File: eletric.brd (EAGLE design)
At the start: 100 x 106.7 mm, 13 parts, among them U1 ATTINY85-20PU

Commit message: smyle?
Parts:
- moved R7 4.96 mm to (61.0, 84.5), turned to 195 degrees
- moved R6 3.70 mm to (56.5, 83.2), turned to 190 degrees
- moved R2 3.42 mm to (38.1, 84.5), turned to 165 degrees
- moved R4 2.84 mm to (47.0, 82.5), turned to 175 degrees
- moved R5 2.84 mm to (52.1, 82.5), turned to 185 degrees
- moved R3 2.69 mm to (42.5, 83.2), turned to 170 degrees
- moved LED2 1.27 mm to (49.5, 91.4)
- moved U1 1.27 mm to (45.7, 67.3)
- moved LS1 0.63 mm to (49.5, 5.71)

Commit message: order components && init pcb trail
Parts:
- moved LS1 45.7 mm to (49.5, 51.4), turned to 180 degrees
- moved LS2 43.8 mm to (49.5, 6.99), turned to 180 degrees
- moved LS3 16.5 mm to (49.5, 34.3), turned to 180 degrees
- moved LS4 15.9 mm to (49.5, 19.7), turned to 180 degrees
- moved R2 2.01 mm to (38.7, 86.4), turned to 135 degrees
- moved R7 2.01 mm to (60.3, 86.4), turned to 225 degrees
- moved R3 0.63 mm to (42.5, 83.8), turned to 155 degrees
- moved R6 0.63 mm to (56.5, 83.8), turned to 205 degrees
- turned R4 to 170 degrees
- turned R5 to 190 degrees
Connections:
- net BUZER_HARMONY_1: now also U1.7; no longer U1.5
- net BUZER_HARMONY_3: now also U1.5; no longer U1.7
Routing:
- net BUZER_HARMONY_1: track 0.00 -> 91.9 mm
- net N$3: track 0.00 -> 88.8 mm
- net N$2: track 0.00 -> 74.5 mm
- net BUZER_HARMONY_2: track 0.00 -> 68.4 mm
- net VOLUME: track 0.00 -> 62.9 mm
- net N$4: track 0.00 -> 62.5 mm
- net N$6: track 0.00 -> 60.4 mm
- net VCC: track 0.00 -> 57.5 mm
- net BUZER_HARMONY_3: track 0.00 -> 53.9 mm
- net GND: track 0.00 -> 46.5 mm
- net BUZER_MELODY: track 0.00 -> 43.8 mm
- net RESET: track 0.00 -> 40.0 mm
- net LED: track 0.00 -> 19.6 mm
- net N$5: track 0.00 -> 18.0 mm

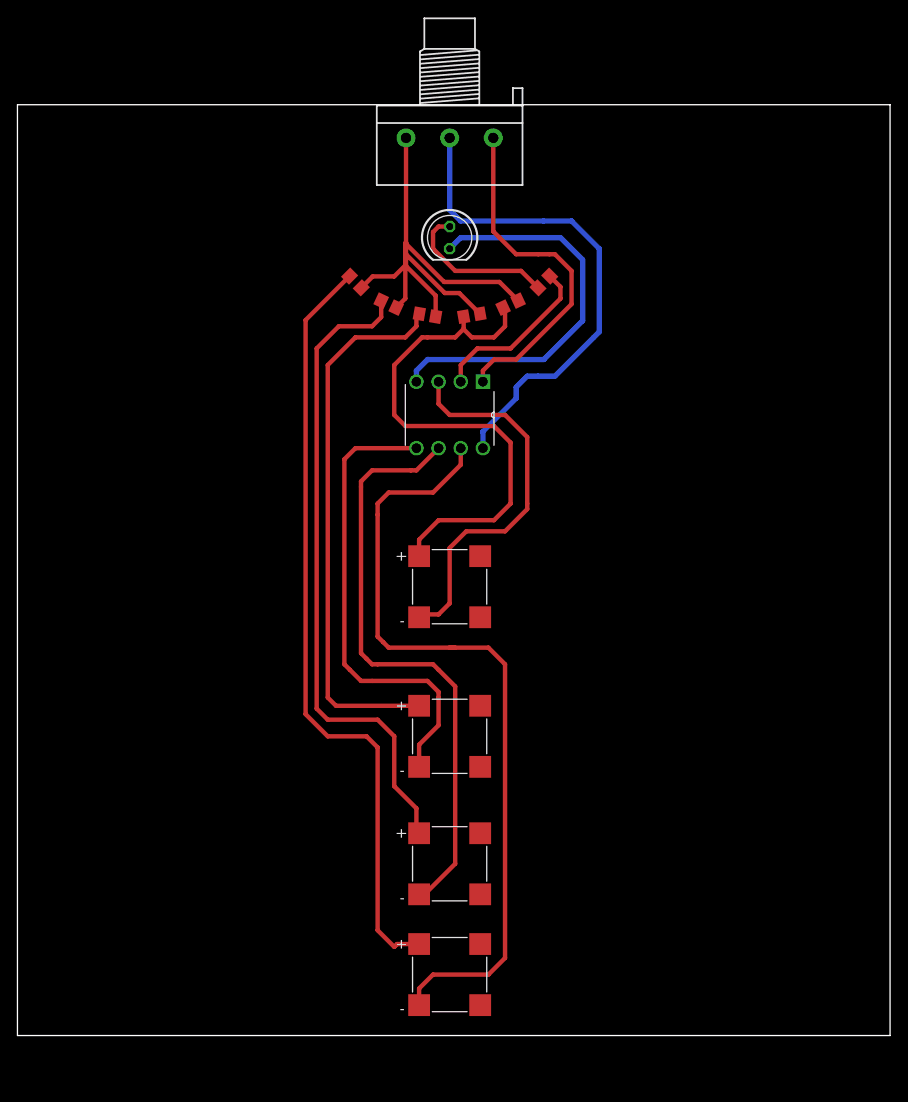
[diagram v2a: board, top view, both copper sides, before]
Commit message: add power circuit
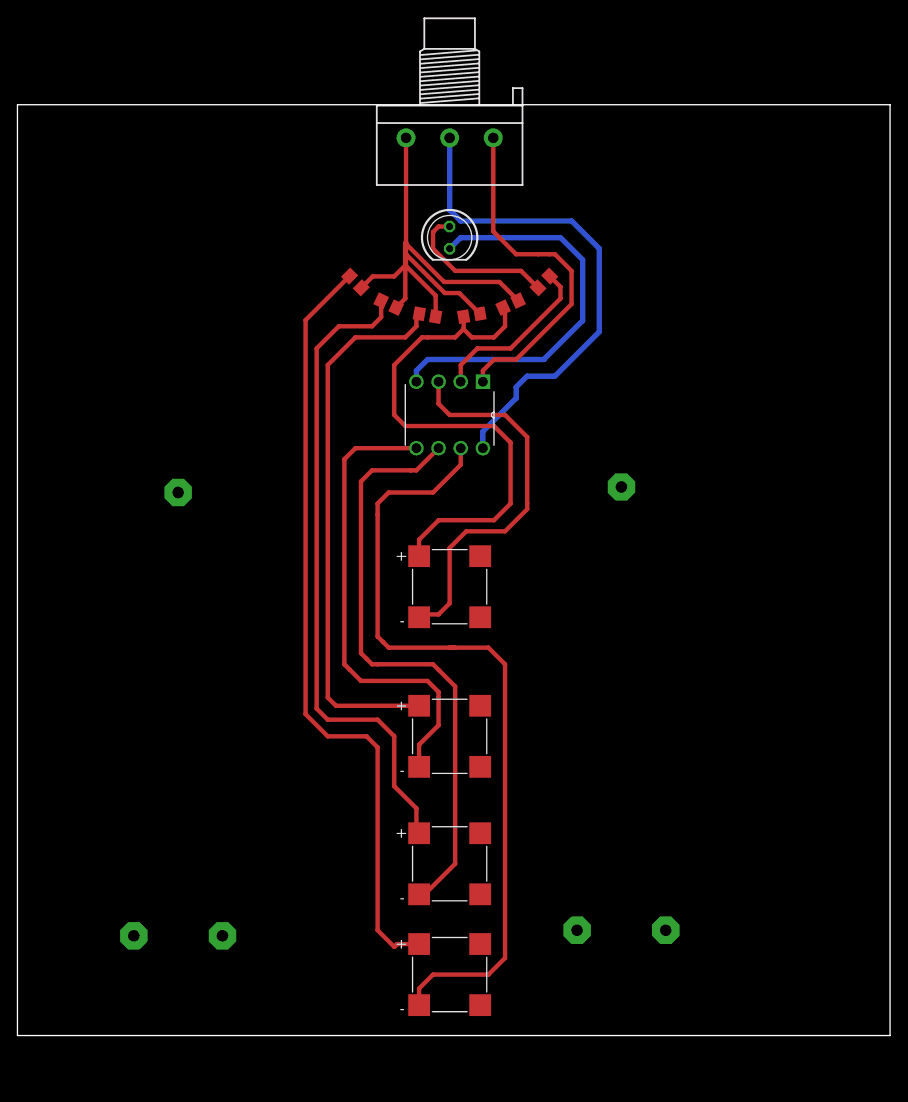
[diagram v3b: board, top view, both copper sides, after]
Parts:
- added G1, G2: CR-AA, battery:CRAA
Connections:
- new net N$1: G1.-, G2.+
- net GND: now also G2.-
- net VCC: now also G1.+
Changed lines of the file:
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@@
 <attribute name="VALUE" x="58.97795625" y="88.605053125" size="1.27" layer="27" rot="R225"/>
+</element>
+<element name="G1" library="battery" library_urn="urn:adsk.eagle:library:109" package="CRAA" package3d_urn="urn:adsk.eagle:package:4582/2" value="CR-AA" x="69.215" y="37.465" smashed="yes" rot="MR90">
+<attribute name="NAME" x="77.47" y="12.065" size="1.27" layer="26" ratio="10" rot="MR90"/>
+<attribute name="POPULARITY" value="0" x="69.215" y="37.465" size="1.778" layer="28" rot="MR90" display="off"/>
+<attribute name="VALUE" x="73.025" y="29.845" size="1.27" layer="28" ratio="10" rot="MR90"/>
+</element>
+<element name="G2" library="battery" library_urn="urn:adsk.eagle:library:109" package="CRAA" package3d_urn="urn:adsk.eagle:package:4582/2" value="CR-AA" x="18.415" y="36.83" smashed="yes" rot="MR90">
+<attribute name="NAME" x="26.67" y="11.43" size="1.27" layer="26" ratio="10" rot="MR90"/>
+<attribute name="POPULARITY" value="0" x="18.415" y="36.83" size="1.778" layer="28" rot="MR90" display="off"/>
+<attribute name="VALUE" x="22.225" y="29.21" size="1.27" layer="28" ratio="10" rot="MR90"/>
 </element>
 </elements>
@@
 <wire x1="57.15" y1="73.025" x2="57.15" y2="74.295" width="0.6096" layer="16"/>
 <wire x1="57.15" y1="74.295" x2="58.42" y2="75.565" width="0.6096" layer="16"/>
-<wire x1="58.42" y1="75.565" x2="59.69" y2="75.565" width="0.6096" layer="16"/>
-<wire x1="59.69" y1="75.565" x2="61.595" y2="75.565" width="0.6096" layer="16"/>
-<wire x1="61.595" y1="75.565" x2="66.04" y2="80.01" width="0.6096" layer="16"/>
-<wire x1="66.04" y1="80.01" x2="66.675" y2="80.645" width="0.6096" layer="16"/>
+<wire x1="58.42" y1="75.565" x2="61.595" y2="75.565" width="0.6096" layer="16"/>
+<wire x1="61.595" y1="75.565" x2="66.675" y2="80.645" width="0.6096" layer="16"/>
 <wire x1="66.675" y1="80.645" x2="66.675" y2="90.17" width="0.6096" layer="16"/>
 <wire x1="66.675" y1="90.17" x2="63.5" y2="93.345" width="0.6096" layer="16"/>
-<wire x1="63.5" y1="93.345" x2="60.325" y2="93.345" width="0.6096" layer="16"/>
-<wire x1="60.325" y1="93.345" x2="50.8" y2="93.345" width="0.6096" layer="16"/>
+<wire x1="63.5" y1="93.345" x2="50.8" y2="93.345" width="0.6096" layer="16"/>
 <wire x1="50.8" y1="93.345" x2="49.53" y2="94.615" width="0.6096" layer="16"/>
 <wire x1="49.53" y1="94.615" x2="49.53" y2="102.87" width="0.6096" layer="16"/>
+<contactref element="G1" pad="+"/>
+<wire x1="64.135" y1="12.065" x2="53.34" y2="67.31" width="0" layer="19" extent="1-1"/>
 </signal>
 <signal name="GND">
@@
 <wire x1="60.325" y1="77.47" x2="64.77" y2="81.915" width="0.6096" layer="16"/>
 <wire x1="49.53" y1="90.17" x2="50.8" y2="91.44" width="0.6096" layer="16"/>
-<wire x1="50.8" y1="91.44" x2="60.325" y2="91.44" width="0.6096" layer="16"/>
-<wire x1="60.325" y1="91.44" x2="62.23" y2="91.44" width="0.6096" layer="16"/>
+<wire x1="50.8" y1="91.44" x2="62.23" y2="91.44" width="0.6096" layer="16"/>
 <wire x1="62.23" y1="91.44" x2="64.77" y2="88.9" width="0.6096" layer="16"/>
 <wire x1="64.77" y1="81.915" x2="64.77" y2="88.9" width="0.6096" layer="16"/>
+<contactref element="G2" pad="-"/>
+<wire x1="18.415" y1="62.23" x2="45.72" y2="74.93" width="0" layer="19" extent="1-1"/>
 </signal>
 <signal name="LED">
@@
 <wire x1="48.26" y1="59.055" x2="46.03" y2="56.825" width="0.508" layer="1"/>
 </signal>
+<signal name="N$1">
+<contactref element="G1" pad="-"/>
+<contactref element="G2" pad="+"/>
+<wire x1="13.335" y1="11.43" x2="69.215" y2="62.865" width="0" layer="19" extent="1-1"/>
+</signal>
 </signals>

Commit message: pcb improve layout
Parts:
- removed LED2: (no value), led:LED5MM
- added LED1: (no value), led:LED3MM
- moved G2 19.1 mm to (36.8, 31.8)
- moved LS1 17.2 mm to (50.2, 68.6)
- moved LS3 12.1 mm to (50.2, 46.4)
- moved U1 11.4 mm to (46.4, 78.7)
- moved R2 10.3 mm to (40.6, 96.5), turned to 110 degrees
- moved R7 10.2 mm to (59.7, 96.5), turned to 250 degrees
- moved LS4 8.91 mm to (50.2, 28.6)
- moved R3 8.91 mm to (43.2, 92.7), turned to 140 degrees
- moved R6 8.91 mm to (57.1, 92.7), turned to 220 degrees
- moved R4 8.28 mm to (47.6, 90.8)
- moved R5 8.28 mm to (52.7, 90.8)
- moved G1 8.08 mm to (63.5, 31.8), turned to 270 degrees
- moved R1 6.38 mm to (50.2, 109.2), flipped to the bottom
- moved LS2 4.49 mm to (50.2, 11.4)
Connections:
- net GND: now also LED1.K; no longer LED2.K
- net N$5: now also LED1.A; no longer LED2.A
- net RESET: now also R1.3; no longer R1.1
- net VOLUME: now also R1.1; no longer R1.3
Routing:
- net VOLUME: track 62.9 -> 112.0 mm
- net N$1: track 0.00 -> 34.9 mm
- net GND: track 46.5 -> 70.6 mm
- net VCC: track 57.5 -> 78.9 mm
- net N$4: track 62.5 -> 47.2 mm
- net BUZER_HARMONY_2: track 68.4 -> 82.9 mm
- net BUZER_HARMONY_1: track 91.9 -> 102.2 mm
- net BUZER_HARMONY_3: track 53.9 -> 63.0 mm
- net N$2: track 74.5 -> 66.1 mm
- net RESET: track 40.0 -> 33.0 mm
- net N$5: track 18.0 -> 11.1 mm
- net N$6: track 60.4 -> 62.7 mm
- net LED: track 19.6 -> 18.6 mm
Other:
- board size 100 x 106.7 mm -> 69.4 x 118.6 mm
